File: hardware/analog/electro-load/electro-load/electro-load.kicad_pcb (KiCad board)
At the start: 2 copper layers, 178 x 119 mm, 140 parts, among them J1 AVR-ISP-10, J2 Conn_WallSocket_Earth, J3 INPUT, J4 INPUT, K1 SANYOU_SRD_Form_C, M1 Noctua NF-A14 5V, Q1 2N2222A, Q2 2N2222A, Q3 IPP037N06L3, Q4 IPP037N06L3, Q5 2N2222, Q6 IPP037N06L3, Q7 IPP037N06L3, SW1 RESET, SW2 ROT_ENC, U1 ATmega328P-AU, U10 ADS1115IDGS, U11 ADS1115IDGS, U12 LMV321, U13 LMV321, U14 LM7805_TO220, U2 MCP4725A0T-E_CH, U3 LMV324, U4 RC1602A, U5 LMV324, U6 LMV324, U8 REF5040ID, U9 LMV321

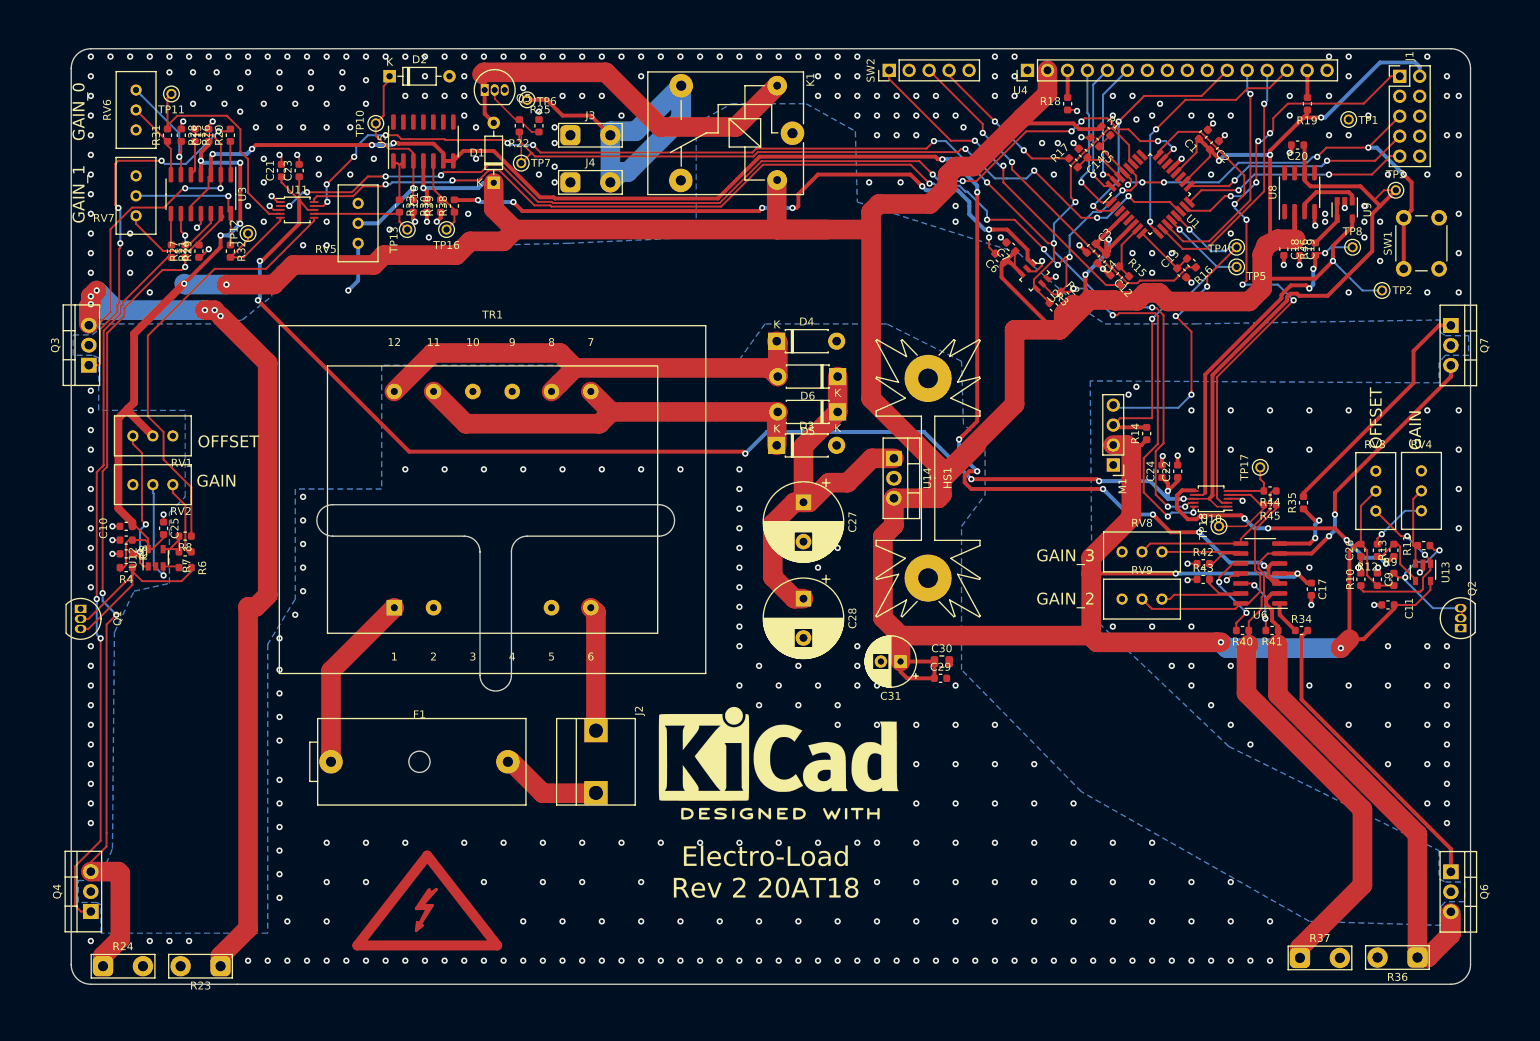
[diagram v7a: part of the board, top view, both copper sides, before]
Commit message: Fixed silkscreen and slighty widened load_current trace.
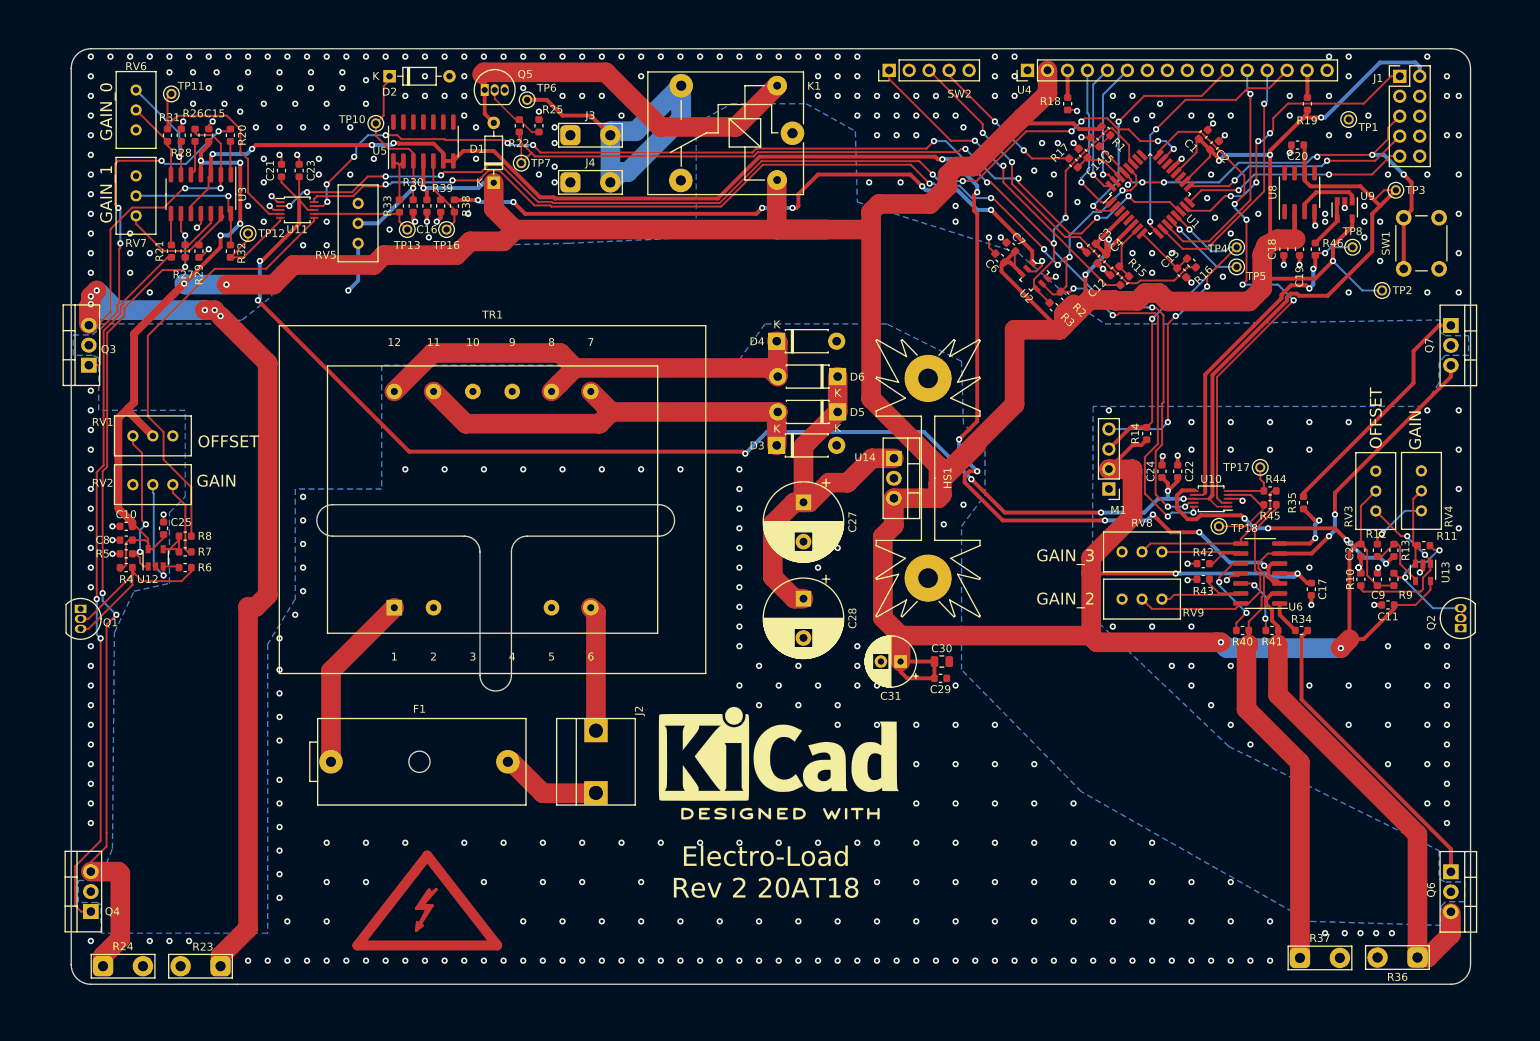
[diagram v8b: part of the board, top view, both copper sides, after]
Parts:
- moved M1 3.10 mm to (194.5, 85.0)
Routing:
- net Net-(Q7-Pad3): track 100.7 -> 94.1 mm
- net /FAN_RPM: track 44.2 -> 41.9 mm
- net +4V: track 238.0 -> 239.5 mm
- net /RELAY_EN: track 99.2 -> 100.3 mm
- net Net-(R16-Pad1): track 47.2 -> 48.2 mm
- net /Current Measurements/CURRENT_SET: track 203.5 -> 204.4 mm
- net /SCL: track 178.9 -> 178.1 mm
- net +5V: track 739.3 -> 738.6 mm
- net GND: vias 481 -> 494
